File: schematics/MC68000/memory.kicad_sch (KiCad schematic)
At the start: 18 parts, among them J1 Conn_02x37_Row_Letter_Last, U13 ROM_LOW, U14 ROM_HIGH, U15 RAM_LOW, U16 RAM_HIGH, U17 GAL20V8, U26 74LS04, U27 74LS574

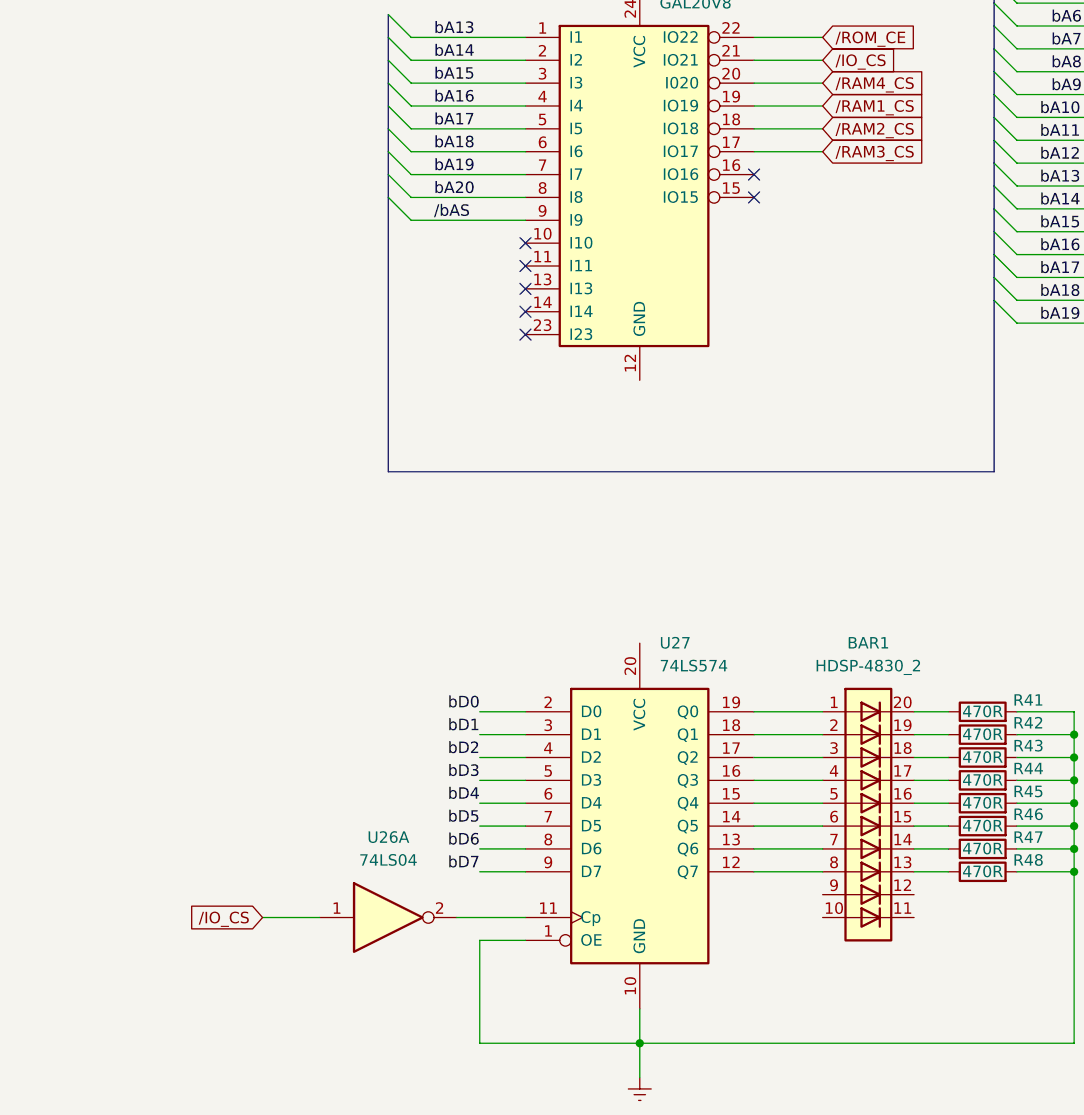
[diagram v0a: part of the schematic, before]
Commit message: update memoria rom executando codigo
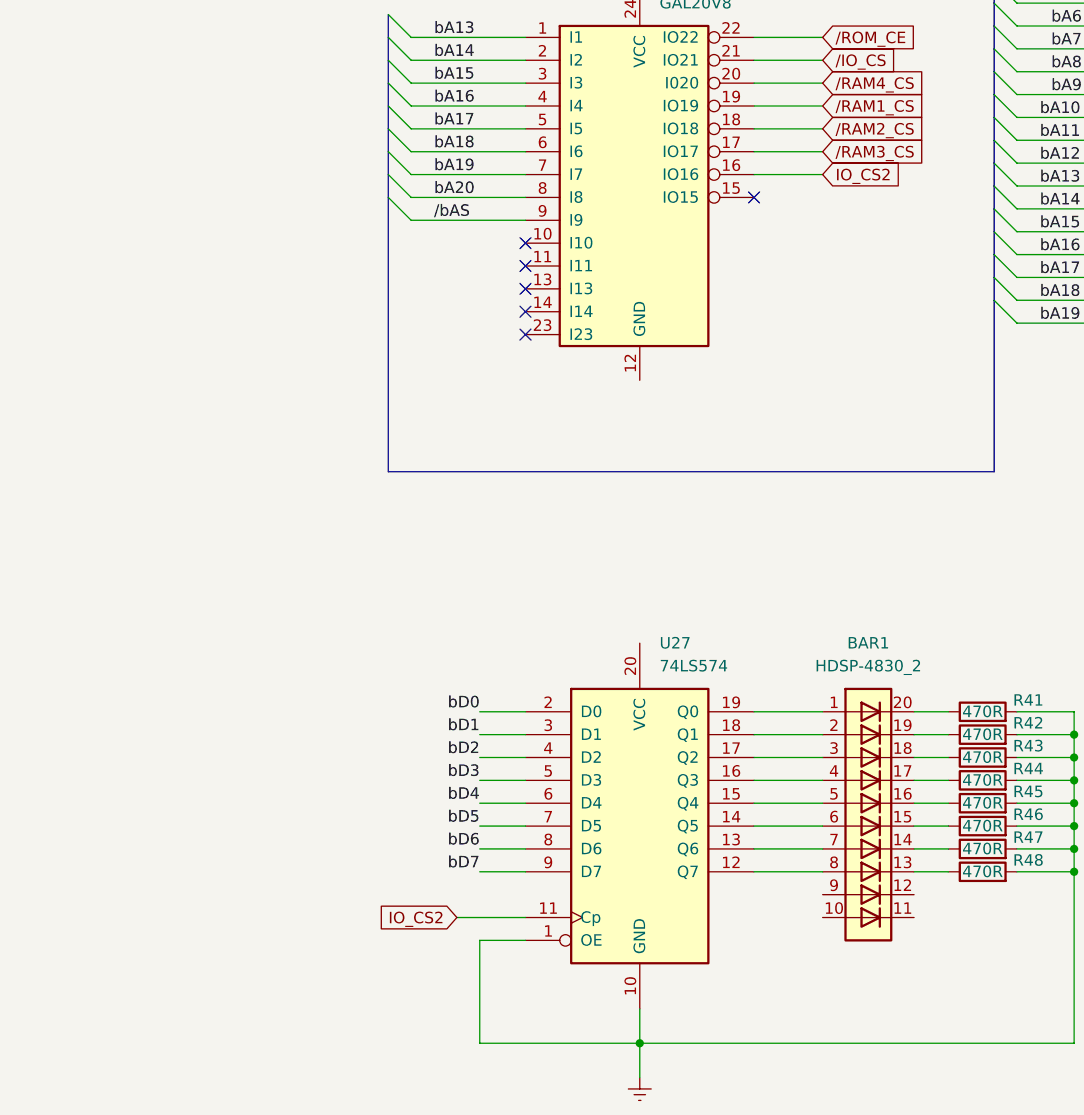
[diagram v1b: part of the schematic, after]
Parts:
- removed unit 1 of U26
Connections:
- net IO_CS2: now reaches U27.11 (Cp)
- net IO_CS2: now also U17.16 (IO16)
- no-connect marks 9 -> 8
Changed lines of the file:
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@@
   )
   (no_connect (at 73.66 140.97))
-  (no_connect (at 99.06 133.35))
   (no_connect (at 73.66 151.13))
   (no_connect (at 201.93 64.77))
@@
     (stroke (width 0) (type default))
   )
+  (wire (pts (xy 106.68 133.35) (xy 99.06 133.35))
+    (stroke (width 0) (type default))
+  )
   (wire (pts (xy 134.62 195.58) (xy 134.62 198.12))
     (stroke (width 0) (type default))
@@
   )
   (wire (pts (xy 242.57 76.2) (xy 254 76.2))
-    (stroke (width 0) (type default))
-  )
-  (wire (pts (xy 44.45 215.9) (xy 50.8 215.9))
     (stroke (width 0) (type default))
   )
@@
     )
   )
+  (global_label "IO_CS2" (shape input) (at 66.04 215.9 180) (fields_autoplaced)
+    (effects (font (size 1.27 1.27)) (justify right))
+    (property "Intersheetrefs" "${INTERSHEET_REFS}" (at 56.4629 215.9 0)
+      (effects (font (size 1.27 1.27)) (justify right) hide)
+    )
+  )
   (global_label "{slash}RAM2_CS" (shape input) (at 106.68 128.27 0) (fields_autoplaced)
     (effects (font (size 1.27 1.27)) (justify left))
@@
     )
   )
+  (global_label "IO_CS2" (shape input) (at 106.68 133.35 0) (fields_autoplaced)
+    (effects (font (size 1.27 1.27)) (justify left))
+    (property "Intersheetrefs" "${INTERSHEET_REFS}" (at 116.2571 133.35 0)
+      (effects (font (size 1.27 1.27)) (justify left) hide)
+    )
+  )
   (global_label "{slash}RAM1_CS" (shape input) (at 106.68 125.73 0) (fields_autoplaced)
     (effects (font (size 1.27 1.27)) (justify left))
@@
     (effects (font (size 1.27 1.27)) (justify right))
     (property "Intersheetrefs" "${INTERSHEET_REFS}" (at 126.6758 67.31 0)
-      (effects (font (size 1.27 1.27)) (justify right) hide)
-    )
-  )
-  (global_label "{slash}IO_CS" (shape input) (at 44.45 215.9 180) (fields_autoplaced)
-    (effects (font (size 1.27 1.27)) (justify right))
-    (property "Intersheetrefs" "${INTERSHEET_REFS}" (at 34.7519 215.9 0)
       (effects (font (size 1.27 1.27)) (justify right) hide)
     )
@@
         )
       )
-    )
-  )
-  (symbol (lib_id "74xx:74LS04") (at 58.42 215.9 0) (unit 1)
-    (in_bom yes) (on_board yes) (dnp no) (fields_autoplaced)
-    (property "Reference" "U26" (at 58.42 207.01 0)
-      (effects (font (size 1.27 1.27)))
-    )
-    (property "Value" "74LS04" (at 58.42 209.55 0)
-      (effects (font (size 1.27 1.27)))
-    )
-    (property "Footprint" "" (at 58.42 215.9 0)
-      (effects (font (size 1.27 1.27)) hide)
-    )
-    (property "Datasheet" "http://www.ti.com/lit/gpn/sn74LS04" (at 58.42 215.9 0)
-      (effects (font (size 1.27 1.27)) hide)
-    )
-    (pin "11")
-    (pin "10")
-    (pin "1")
-    (pin "2")
-    (pin "5")
-    (pin "6")
-    (pin "13")
-    (pin "8")
-    (pin "4")
-    (pin "7")
-    (pin "3")
-    (pin "9")
-    (pin "12")
-    (pin "14")
-    (instances
-      (project "MC68000"
-        (path "/99c9748a-87b3-41bd-bdc2-3a5f137c7a40/46851f42-1a1d-4f27-b9e4-631920caffce"
-          (reference "U26") (unit 1)
-        )
-      )

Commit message: Leds blinking...
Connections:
- net GNDREF: now also U13.22 (~{OE}), U14.22 (~{OE})
- net /DTACK: now also J1.35b (Pin_35b), U17.15 (IO15)
- net /bLDS: no longer U13.22 (~{OE})
- net /bUDS: no longer U14.22 (~{OE})
- net /RAM4_CS: no longer names the net of U17.20 (I020)
- no-connect marks 8 -> 7
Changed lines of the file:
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@@
   (junction (at 134.62 210.82) (diameter 0) (color 0 0 0 0)
   )
+  (junction (at 198.12 78.74) (diameter 0) (color 0 0 0 0)
+  )
   (no_connect (at 73.66 140.97))
   (no_connect (at 73.66 151.13))
   (no_connect (at 201.93 64.77))
   (no_connect (at 73.66 148.59))
-  (no_connect (at 99.06 135.89))
   (no_connect (at 140.97 64.77))
   (no_connect (at 73.66 146.05))
@@
     (stroke (width 0) (type default))
   )
-  (wire (pts (xy 138.43 69.85) (xy 140.97 69.85))
+  (wire (pts (xy 134.62 69.85) (xy 140.97 69.85))
     (stroke (width 0) (type default))
   )
@@
     (stroke (width 0) (type default))
   )
+  (wire (pts (xy 106.68 135.89) (xy 99.06 135.89))
+    (stroke (width 0) (type default))
+  )
   (bus (pts (xy 279.4 78.74) (xy 279.4 81.28))
     (stroke (width 0) (type default))
@@
     (stroke (width 0) (type default))
   )
+  (wire (pts (xy 134.62 69.85) (xy 134.62 78.74))
+    (stroke (width 0) (type default))
+  )
   (bus (pts (xy 278.13 50.8) (xy 278.13 53.34))
     (stroke (width 0) (type default))
@@
     (stroke (width 0) (type default))
   )
+  (wire (pts (xy 134.62 78.74) (xy 198.12 78.74))
+    (stroke (width 0) (type default))
+  )
   (bus (pts (xy 182.88 31.75) (xy 182.88 34.29))
     (stroke (width 0) (type default))
@@
     (stroke (width 0) (type default))
   )
+  (wire (pts (xy 198.12 81.28) (xy 198.12 78.74))
+    (stroke (width 0) (type default))
+  )
   (wire (pts (xy 134.62 208.28) (xy 134.62 210.82))
     (stroke (width 0) (type default))
@@
     (stroke (width 0) (type default))
   )
+  (wire (pts (xy 198.12 69.85) (xy 198.12 78.74))
+    (stroke (width 0) (type default))
+  )
   (bus (pts (xy 125.73 34.29) (xy 125.73 36.83))
     (stroke (width 0) (type default))
@@
     (stroke (width 0) (type default))
   )
+  (wire (pts (xy 271.78 134.62) (xy 266.7 134.62))
+    (stroke (width 0) (type default))
+  )
   (wire (pts (xy 68.58 195.58) (xy 73.66 195.58))
     (stroke (width 0) (type default))
@@
     )
   )
-  (global_label "{slash}bLDS" (shape input) (at 138.43 69.85 180) (fields_autoplaced)
-    (effects (font (size 1.27 1.27)) (justify right))
-    (property "Intersheetrefs" "${INTERSHEET_REFS}" (at 129.4577 69.85 0)
-      (effects (font (size 1.27 1.27)) (justify right) hide)
-    )
-  )
-  (global_label "{slash}RAM4_CS" (shape input) (at 106.68 123.19 0) (fields_autoplaced)
-    (effects (font (size 1.27 1.27)) (justify left))
-    (property "Intersheetrefs" "${INTERSHEET_REFS}" (at 119.4623 123.19 0)
-      (effects (font (size 1.27 1.27)) (justify left) hide)
-    )
-  )
   (global_label "IO_CS2" (shape input) (at 66.04 215.9 180) (fields_autoplaced)
     (effects (font (size 1.27 1.27)) (justify right))
@@
     )
   )
-  (global_label "{slash}bUDS" (shape input) (at 198.12 69.85 180) (fields_autoplaced)
-    (effects (font (size 1.27 1.27)) (justify right))
-    (property "Intersheetrefs" "${INTERSHEET_REFS}" (at 188.8453 69.85 0)
-      (effects (font (size 1.27 1.27)) (justify right) hide)
+  (global_label "{slash}DTACK" (shape input) (at 106.68 135.89 0) (fields_autoplaced)
+    (effects (font (size 1.27 1.27)) (justify left))
+    (property "Intersheetrefs" "${INTERSHEET_REFS}" (at 116.8619 135.89 0)
+      (effects (font (size 1.27 1.27)) (justify left) hide)
     )
   )
@@
     )
   )
+  (global_label "{slash}DTACK" (shape input) (at 271.78 134.62 0) (fields_autoplaced)
+    (effects (font (size 1.27 1.27)) (justify left))
+    (property "Intersheetrefs" "${INTERSHEET_REFS}" (at 281.9619 134.62 0)
+      (effects (font (size 1.27 1.27)) (justify left) hide)
+    )
+  )
   (symbol (lib_id "Memory_RAM:AS6C4008-55PCN") (at 149.86 127 0) (unit 1)
     (in_bom yes) (on_board yes) (dnp no) (fields_autoplaced)
@@
         )
       )
+    )
+  )
+  (symbol (lib_id "power:GNDREF") (at 198.12 81.28 0) (unit 1)
+    (in_bom yes) (on_board yes) (dnp no) (fields_autoplaced)
+    (property "Reference" "#PWR072" (at 198.12 87.63 0)
+      (effects (font (size 1.27 1.27)) hide)
+    )
+    (property "Value" "GNDREF" (at 198.12 86.36 0)
+      (effects (font (size 1.27 1.27)) hide)
+    )
+    (property "Footprint" "" (at 198.12 81.28 0)
+      (effects (font (size 1.27 1.27)) hide)
+    )
+    (property "Datasheet" "" (at 198.12 81.28 0)
+      (effects (font (size 1.27 1.27)) hide)
+    )
+    (pin "1")
+    (instances
+      (project "MC68000"
+        (path "/99c9748a-87b3-41bd-bdc2-3a5f137c7a40/46851f42-1a1d-4f27-b9e4-631920caffce"
+          (reference "#PWR072") (unit 1)
+        )
+      )

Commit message: Ram memory test 2 OK
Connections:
- net /DTACK: no longer J1.28b (Pin_28b)
- net /RAM1_CS: no longer J1.36b (Pin_36b)
- net /ROM_CE: no longer J1.37b (Pin_37b)
- net /RD: now reaches J1.33b (Pin_33b)
- net /RESET: now reaches U17.10 (I10)
- net /RESET: now also J1.37b (Pin_37b)
- net RESET: now reaches U17.20 (I020)
- net RESET: now also J1.36b (Pin_36b)
- net /bR/W renamed bR/W
- no-connect marks 7 -> 6
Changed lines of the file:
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@@
   (junction (at 198.12 78.74) (diameter 0) (color 0 0 0 0)
   )
-  (no_connect (at 73.66 140.97))
   (no_connect (at 73.66 151.13))
   (no_connect (at 201.93 64.77))
@@
     (stroke (width 0) (type default))
   )
-  (bus_entry (at 283.21 114.3) (size -2.54 2.54)
-    (stroke (width 0) (type default))
-  )
   (bus_entry (at 58.42 120.65) (size 2.54 2.54)
     (stroke (width 0) (type default))
@@
     (stroke (width 0) (type default))
   )
+  (wire (pts (xy 271.78 129.54) (xy 266.7 129.54))
+    (stroke (width 0) (type default))
+  )
   (wire (pts (xy 238.76 124.46) (xy 254 124.46))
     (stroke (width 0) (type default))
@@
     (stroke (width 0) (type default))
   )
+  (wire (pts (xy 71.12 140.97) (xy 73.66 140.97))
+    (stroke (width 0) (type default))
+  )
   (bus (pts (xy 240.03 78.74) (xy 240.03 81.28))
     (stroke (width 0) (type default))
@@
   )
   (bus (pts (xy 240.03 44.45) (xy 240.03 45.72))
-    (stroke (width 0) (type default))
-  )
-  (wire (pts (xy 280.67 116.84) (xy 266.7 116.84))
     (stroke (width 0) (type default))
   )
@@
   )
   (label "bA6" (at 132.08 116.84 0) (fields_autoplaced)
-    (effects (font (size 1.27 1.27)) (justify left bottom))
-  )
-  (label "{slash}DTACK" (at 266.7 116.84 0) (fields_autoplaced)
     (effects (font (size 1.27 1.27)) (justify left bottom))
   )
@@
     )
   )
-  (global_label "{slash}RAM1_CS" (shape input) (at 271.78 137.16 0) (fields_autoplaced)
-    (effects (font (size 1.27 1.27)) (justify left))
-    (property "Intersheetrefs" "${INTERSHEET_REFS}" (at 284.5623 137.16 0)
-      (effects (font (size 1.27 1.27)) (justify left) hide)
-    )
-  )
   (global_label "{slash}RAM1_CS" (shape input) (at 165.1 129.54 0) (fields_autoplaced)
     (effects (font (size 1.27 1.27)) (justify left))
@@
     )
   )
-  (global_label "{slash}ROM_CE" (shape input) (at 271.78 139.7 0) (fields_autoplaced)
-    (effects (font (size 1.27 1.27)) (justify left))
-    (property "Intersheetrefs" "${INTERSHEET_REFS}" (at 283.5342 139.7 0)
-      (effects (font (size 1.27 1.27)) (justify left) hide)
-    )
-  )
   (global_label "{slash}bLDS" (shape input) (at 165.1 132.08 0) (fields_autoplaced)
     (effects (font (size 1.27 1.27)) (justify left))
@@
     )
   )
+  (global_label "{slash}RESET" (shape input) (at 271.78 139.7 0) (fields_autoplaced)
+    (effects (font (size 1.27 1.27)) (justify left))
+    (property "Intersheetrefs" "${INTERSHEET_REFS}" (at 281.8408 139.7 0)
+      (effects (font (size 1.27 1.27)) (justify left) hide)
+    )
+  )
   (global_label "IO_CS2" (shape input) (at 66.04 215.9 180) (fields_autoplaced)
     (effects (font (size 1.27 1.27)) (justify right))
@@
     )
   )
+  (global_label "RESET" (shape input) (at 271.78 137.16 0) (fields_autoplaced)
+    (effects (font (size 1.27 1.27)) (justify left))
+    (property "Intersheetrefs" "${INTERSHEET_REFS}" (at 280.5103 137.16 0)
+      (effects (font (size 1.27 1.27)) (justify left) hide)
+    )
+  )
   (global_label "{slash}DTACK" (shape input) (at 106.68 135.89 0) (fields_autoplaced)
     (effects (font (size 1.27 1.27)) (justify left))
@@
     )
   )
-  (global_label "{slash}bR{slash}W" (shape input) (at 165.1 134.62 0) (fields_autoplaced)
+  (global_label "{slash}RESET" (shape input) (at 71.12 140.97 180) (fields_autoplaced)
+    (effects (font (size 1.27 1.27)) (justify right))
+    (property "Intersheetrefs" "${INTERSHEET_REFS}" (at 61.0592 140.97 0)
+      (effects (font (size 1.27 1.27)) (justify right) hide)
+    )
+  )
+  (global_label "bR{slash}W" (shape input) (at 165.1 134.62 0) (fields_autoplaced)
     (effects (font (size 1.27 1.27)) (justify left))
-    (property "Intersheetrefs" "${INTERSHEET_REFS}" (at 174.6166 134.62 0)
+    (property "Intersheetrefs" "${INTERSHEET_REFS}" (at 173.2861 134.62 0)
       (effects (font (size 1.27 1.27)) (justify left) hide)
     )
@@
     )
   )
-  (global_label "{slash}bR{slash}W" (shape input) (at 226.06 134.62 0) (fields_autoplaced)
+  (global_label "{slash}RD" (shape input) (at 271.78 129.54 0) (fields_autoplaced)
     (effects (font (size 1.27 1.27)) (justify left))
-    (property "Intersheetrefs" "${INTERSHEET_REFS}" (at 235.5766 134.62 0)
+    (property "Intersheetrefs" "${INTERSHEET_REFS}" (at 278.6357 129.54 0)
       (effects (font (size 1.27 1.27)) (justify left) hide)
     )
+  )
+  (global_label "bR{slash}W" (shape input) (at 226.06 134.62 0) (fields_autoplaced)
+    (effects (font (size 1.27 1.27)) (justify left))
+    (property "Intersheetrefs" "${INTERSHEET_REFS}" (at 234.2461 134.62 0)
+      (effects (font (size 1.27 1.27)) (justify left) hide)
+    )
+  )
+  (global_label "RESET" (shape input) (at 106.68 123.19 0) (fields_autoplaced)
+    (effects (font (size 1.27 1.27)) (justify left))
+    (property "Intersheetrefs" "${INTERSHEET_REFS}" (at 115.4103 123.19 0)
+      (effects (font (size 1.27 1.27)) (justify left) hide)
+    )
